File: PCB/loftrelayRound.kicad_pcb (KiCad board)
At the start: 2 copper layers, 70.1 x 70.1 mm, 27 parts, among them J1 PowerIn, J2 Load, J3 SenSor, J4 Program, K1 G5Q-14-EU DC5, Q1 2N7002, U1 AP1117-33, U2 PC817, U4 ESP-12E

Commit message: 3d footprint
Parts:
- K1: footprint Relays_THT:Relay_SPST_OMRON-G5Q -> Relay_THT:Relay_SPST_Omron-G5Q-1A
- Q1: value 2N7002 -> Sq2318AES
- R1: value 10k -> 33K
- R8: value 10k -> 33k

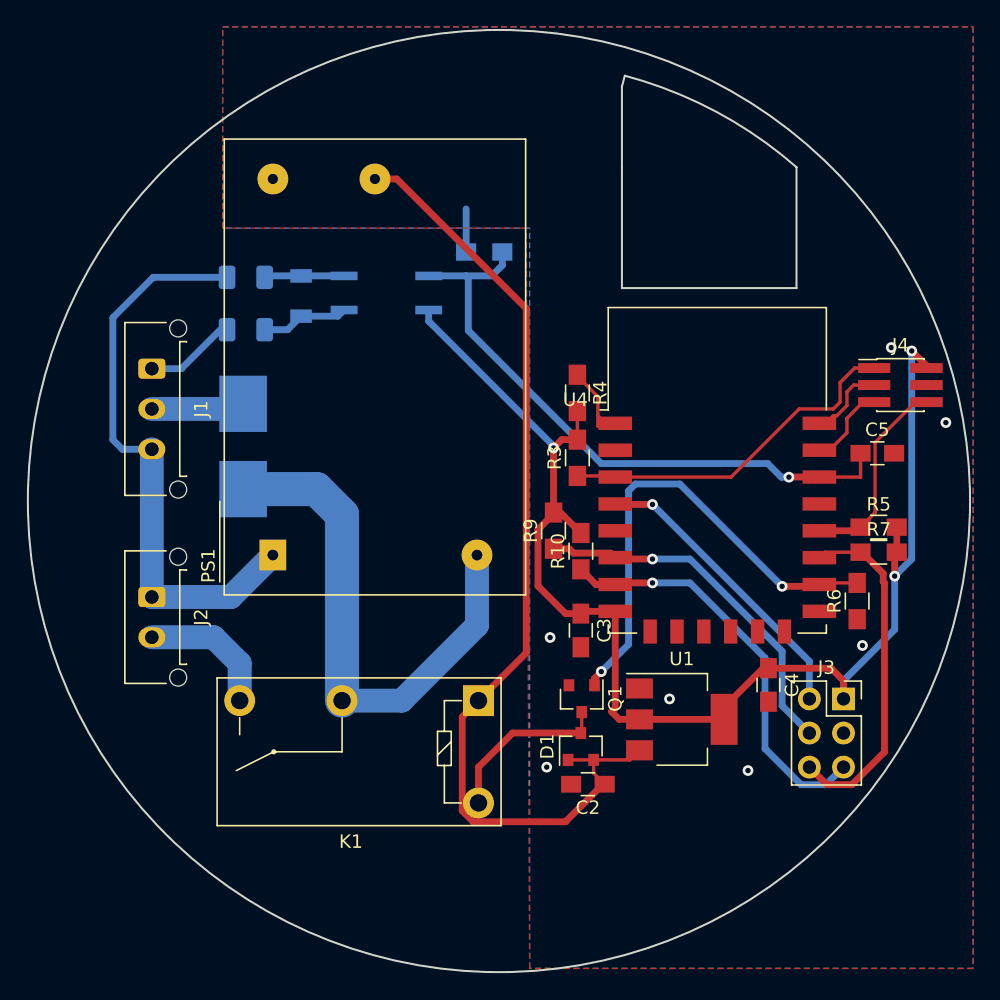
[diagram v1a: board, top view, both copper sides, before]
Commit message: Final edit
Ændret LDO , da jeg ikke kunne skaffe den anden på mouser kun i kina, hvilket jeg ikke har tid til. Rettet en bane der kom lidt for tæt og fejlede i første forsøg
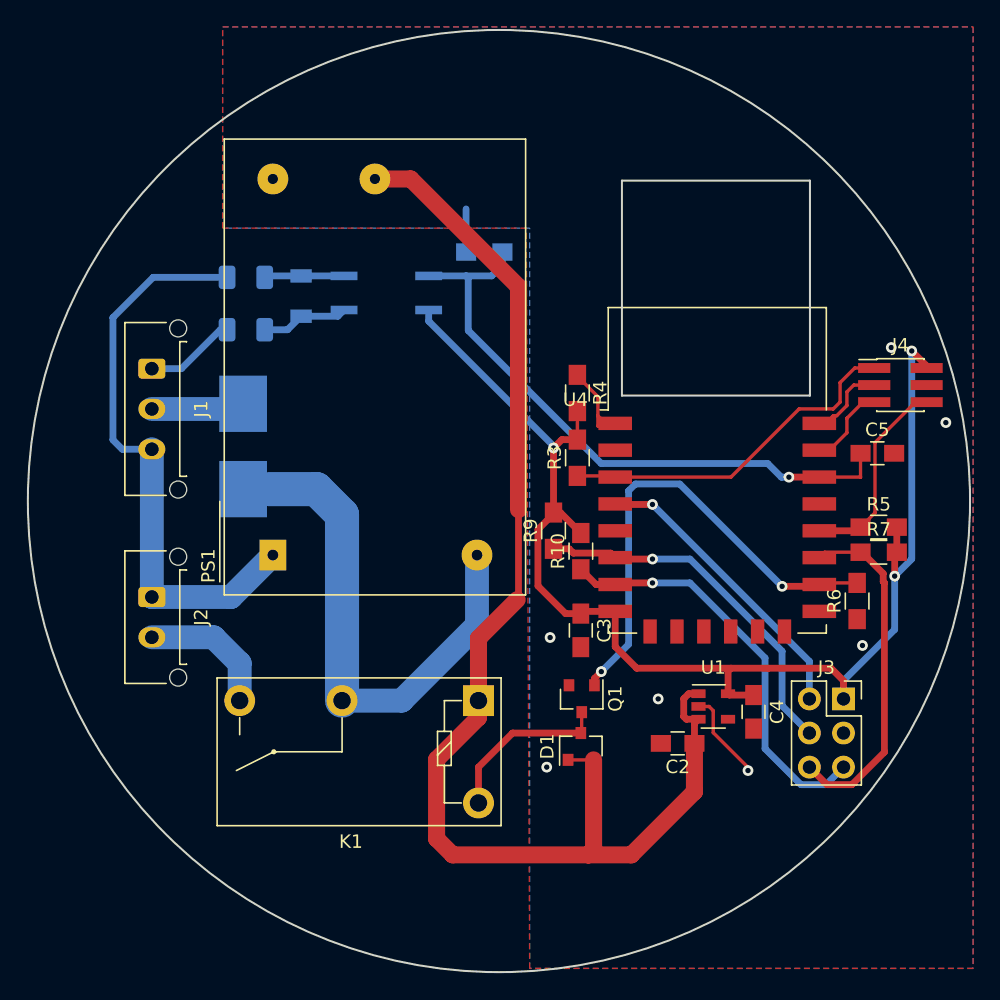
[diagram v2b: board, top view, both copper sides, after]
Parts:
- C2: value 22uF -> 1uF
- U1: value AP1117-33 -> AP2112K-3.3; footprint Package_TO_SOT_SMD:SOT-223-3_TabPin2 -> Package_TO_SOT_SMD:SOT-23-5
- moved C2 7.34 mm to (162.2, 135.9)
- moved U1 2.53 mm to (164.8, 133.2)
- moved C4 2.29 mm to (167.8, 133.6)
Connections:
- U1 pad 1: GNDD -> +5V
- U1 pad 2: +3V3 -> GNDD
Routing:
- net +5V: track 75.1 -> 98.3 mm
- net GNDD: track 3.21 -> 9.97 mm
- net +3V3: track 100.8 -> 97.8 mm
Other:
- outline, holes or cut-outs redrawn

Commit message: Update referance
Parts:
- C3, C4: value 22uF -> 1uF
- R1: value 33K -> 100k
- R8: value 33k -> 100k
- U2: value PC817 -> LTV-355T
